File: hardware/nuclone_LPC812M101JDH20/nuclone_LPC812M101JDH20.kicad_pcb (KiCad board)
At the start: 2 copper layers, 48.3 x 48.3 mm, 102 parts, among them J1 JTAG_2X05, J2 Conn_01x02, J2 USB-ID, J3 nuclone_small_left, J4 nuclone_small_right, U1 MCP1702-MB, U1 USBLC6-2, U2 LPC812M101JDH20, U2 MCP1702-MB, U3 LPC812M101JDH20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

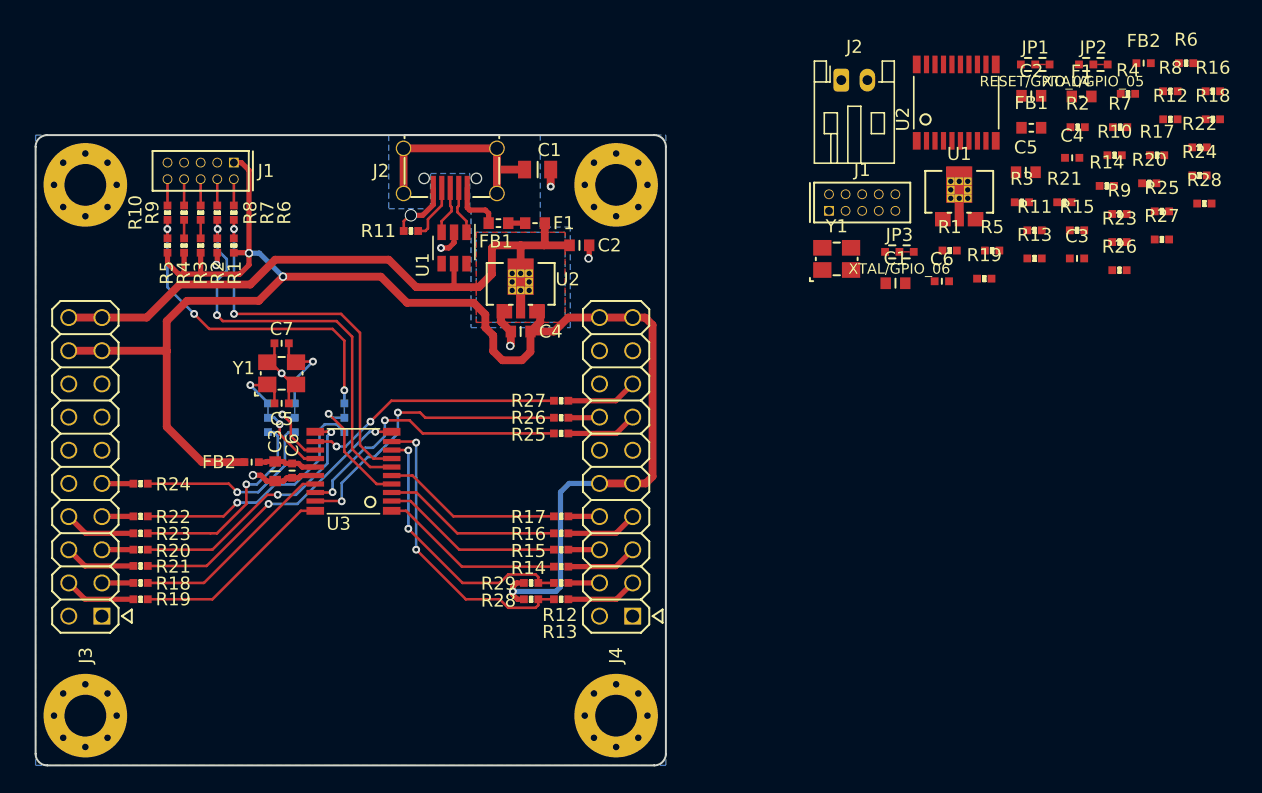
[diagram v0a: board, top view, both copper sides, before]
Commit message: newer footprints for nuclone generic, some updates to pcb
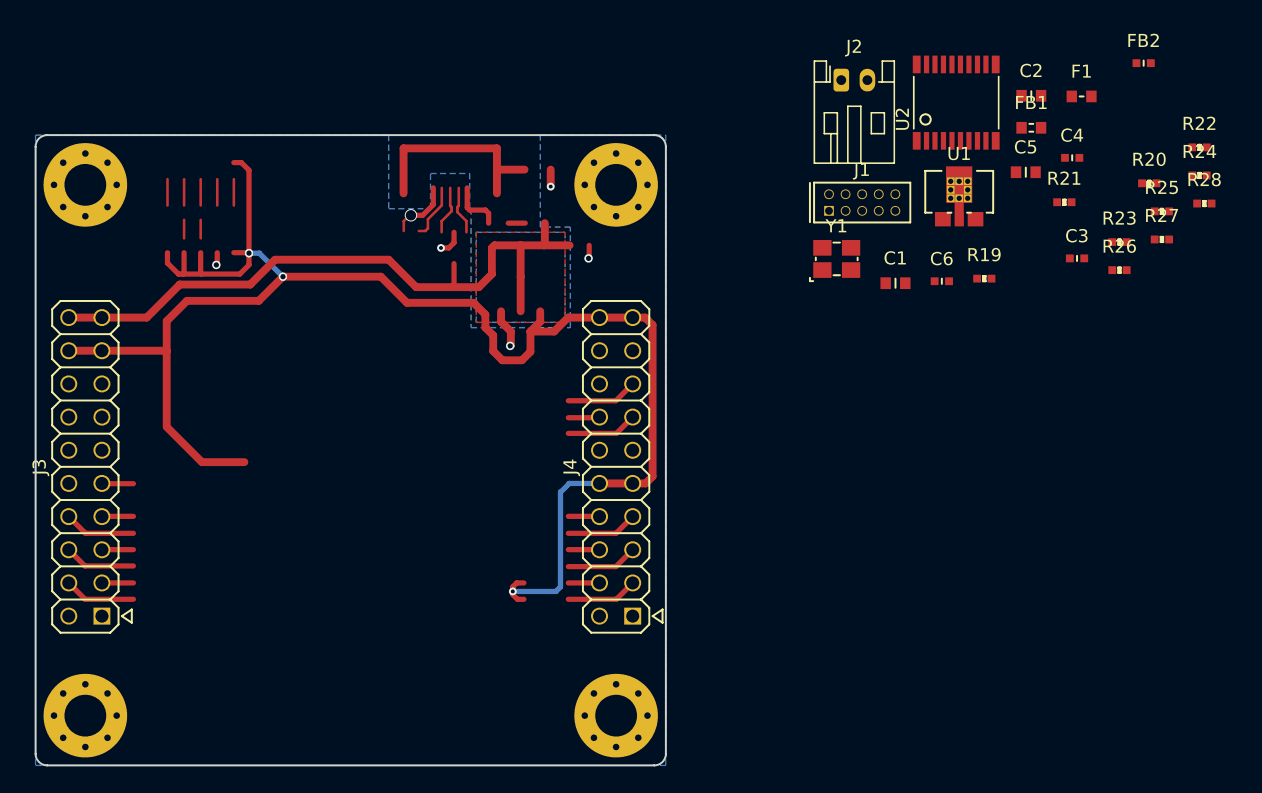
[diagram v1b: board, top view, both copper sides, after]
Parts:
- removed the C1 at (99.4, 63.6)
- removed the C2 at (102.6, 69.4)
- removed the C3 at (79.3, 86.7)
- removed the C4 at (98.1, 76.0)
- removed the C5 at (79.8, 81.5)
- removed the C6 at (80.6, 86.7)
- removed C7: 18p, SquantorRcl:C_0402
- removed the F1 at (99.2, 67.7)
- removed the FB1 at (96.4, 67.7)
- removed the FB2 at (77.5, 86.0)
- removed the J1 at (73.6, 63.7)
- removed the J2 at (92.7, 63.7)
- removed JP1 (x2): RESET/GPIO_04, SquantorSpecial:solder_jumper_3way_23conn
- removed JP2 (x2): XTAL/GPIO_05, SquantorSpecial:solder_jumper_3way_23conn
- removed JP3 (x2): XTAL/GPIO_06, SquantorSpecial:solder_jumper_3way_23conn
- removed R1, R10 (x2), R11, R12 (x2), R13 (x2), R14 (x2), R15 (x2), R16 (x2), R17, R18, R2, R3, R4, R5, R6 (x2), R7 (x2), R8 (x2), R9 (x2): 100, SquantorRcl:R_0402_hand
- removed R1, R4: 100K, SquantorRcl:R_0402_hand
- removed R11: 0, SquantorRcl:R_0402_hand
- removed R17, R18, R29: 2.2K, SquantorRcl:R_0402_hand
- removed the R19 at (69.0, 96.5)
- removed R2, R3, R5: 100k, SquantorRcl:R_0402_hand
- removed the R20 at (69.0, 92.7)
- removed the R21 at (69.0, 94.0)
- removed the R22 at (69.0, 90.2)
- removed the R23 at (69.0, 91.5)
- removed the R24 at (69.0, 87.7)
- removed the R25 at (101.2, 83.8)
- removed the R26 at (101.2, 82.6)
- removed the R27 at (101.2, 81.3)
- removed the R28 at (98.9, 96.5)
- removed the U1 at (93.0, 69.6)
- removed the U2 at (98.1, 72.7)
- removed U3: LPC812M101JDH20, SquantorIC:SOT360
- removed the Y1 at (79.8, 79.2)
- J3: footprint SquantorConnectorsNamed:Nuclone_20pin_gpio -> SquantorConnectorsNamed:nuclone_small_left
- J4: footprint SquantorConnectorsNamed:Nuclone_20pin_bus_analog -> SquantorConnectorsNamed:nuclone_small_right
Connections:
- net /MCU_RESET renamed /RESET
- C2 pad 1: /VBUS -> VSS
- C2 pad 2: VSS -> /VBUS
- J2 pad 1: (no net) -> VSS
- J2 pad 2: (no net) -> Net-(FB1-Pad2)
- J4 pad 19: (no net) -> /VDD
- J4 pad 20: (no net) -> /VDD
- U2 pad 1: /PIO0_17 -> (no net)
- U2 pad 10: /PIO0_16 -> (no net)
- U2 pad 11: /PIO0_15 -> (no net)
- U2 pad 12: /PIO0_1 -> (no net)
- U2 pad 13: /PIO0_9 -> (no net)
- U2 pad 14: /PIO0_8 -> (no net)
- U2 pad 17: /PIO0_7 -> (no net)
- U2 pad 18: /PIO0_6 -> (no net)
- U2 pad 19: /PIO0_0 -> (no net)
- U2 pad 2: /PIO0_13 -> (no net)
- U2 pad 20: /PIO0_14 -> (no net)
- U2 pad 3: /PIO0_12 -> (no net)
- U2 pad 4: /PIO0_5 -> (no net)
- U2 pad 5: /PIO0_4 -> (no net)
- U2 pad 8: /PIO0_11 -> (no net)
- U2 pad 9: /PIO0_10 -> (no net)
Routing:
- net (no net): track 5.46 -> 62.9 mm
- net /MCU_TCK: track 31.9 -> 0.00 mm, vias 2 -> 0
- net /MCU_TMS: track 29.6 -> 0.00 mm, vias 2 -> 0
- net /RESET: track 25.9 -> 0.00 mm, vias 3 -> 0
- net /LPC812M101JD20 base/PIO0_10: track 23.0 -> 0.00 mm, vias 2 -> 0
- net /LPC812M101JD20 base/PIO0_0: track 23.0 -> 0.00 mm, vias 2 -> 0
- net /LPC812M101JD20 base/PIO0_16: track 22.9 -> 0.00 mm, vias 2 -> 0
- net /LPC812M101JD20 base/PIO0_6: track 22.2 -> 0.00 mm, vias 2 -> 0
- net /LPC812M101JD20 base/PIO0_11: track 21.0 -> 0.00 mm, vias 2 -> 0
- net /LPC812M101JD20 base/PIO0_15: track 20.3 -> 0.00 mm, vias 2 -> 0
- net /LPC812M101JD20 base/PIO0_1: track 19.9 -> 0.00 mm, vias 2 -> 0
- net /LPC812M101JD20 base/GPIO_04_INT: track 19.6 -> 0.00 mm, vias 1 -> 0
- net /LPC812M101JD20 base/GPIO_05_INT: track 16.0 -> 0.00 mm, vias 1 -> 0
- net /LPC812M101JD20 base/PIO0_7: track 16.0 -> 0.00 mm
- net /LPC812M101JD20 base/PIO0_14: track 15.6 -> 0.00 mm
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
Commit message: updated footprints for the connectors (again)
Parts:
- removed R19, R22: 100K, SquantorRcl:R_0402_hand
- removed R20, R21, R23: 100k, SquantorRcl:R_0402_hand
- removed R24, R25, R26, R27, R28: 100, SquantorRcl:R_0402_hand
- J4: value nuclone_small_right -> Header-0254-2X10-H010
- moved F1 50.4 mm to (91.0, 64.0), turned to 270 degrees
- moved FB1 46.7 mm to (91.0, 67.0), turned to 270 degrees
- moved J2 28.0 mm to (96.9, 67.7), turned to 180 degrees
- turned J3 to 270 degrees
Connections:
- J1 pad 10: Net-(J1-Pad10) -> (no net)
- J1 pad 2: Net-(J1-Pad2) -> (no net)
- J1 pad 4: Net-(J1-Pad4) -> (no net)
- J1 pad 6: Net-(J1-Pad6) -> (no net)
- J1 pad 8: Net-(J1-Pad8) -> (no net)
- J3 pad 1: VSS -> /VDD
- J3 pad 17: /VDD -> (no net)
- J3 pad 18: /VDD -> (no net)
- J3 pad 19: /VBUS -> (no net)
- J3 pad 2: VSS -> /VDD
- J3 pad 20: /VBUS -> (no net)
- J3 pad 3: (no net) -> /VBUS
- J3 pad 4: (no net) -> /VBUS
- J3 pad 5: (no net) -> VSS
- J3 pad 6: (no net) -> VSS
- J4 pad 1: VSS -> (no net)
- J4 pad 17: (no net) -> VSS
- J4 pad 18: (no net) -> VSS
- J4 pad 2: VSS -> (no net)
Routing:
- net /VDD: track 126.5 -> 0.00 mm, vias 3 -> 0
- net (no net): track 62.9 -> 0.17 mm
- net /VBUS: track 52.2 -> 0.00 mm
- net Net-(C1-Pad1): track 16.2 -> 0.00 mm
- net VSS: track 13.1 -> 0.00 mm, vias 6 -> 0
- net Net-(J2-Pad4): track 4.32 -> 0.00 mm
- net Net-(FB1-Pad2): track 4.08 -> 0.00 mm
- net /USB input/USB_IN_D+: track 3.76 -> 0.00 mm
- net /USB input/USB_IN_D-: track 3.73 -> 0.00 mm
- net Net-(J1-Pad8): track 2.02 -> 0.00 mm
- net Net-(J1-Pad6): track 2.02 -> 0.00 mm
- net Net-(J1-Pad4): track 2.02 -> 0.00 mm
- net Net-(J1-Pad2): track 2.02 -> 0.00 mm
- net Net-(J1-Pad10): track 2.02 -> 0.00 mm
- net /MCU_TDO: track 1.41 -> 0.00 mm
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- removed copper zone on B.Cu, net /VBUS
- removed copper zone on F.Cu, net /VBUS

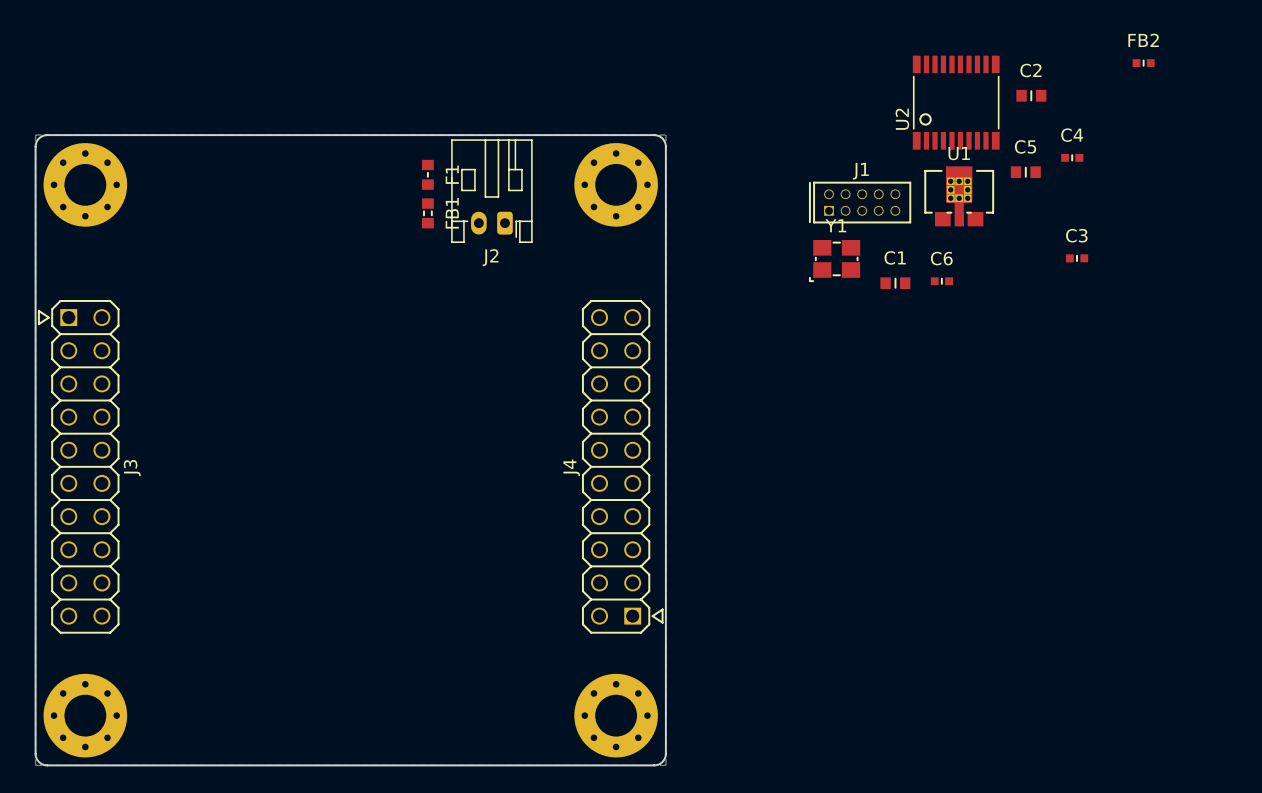
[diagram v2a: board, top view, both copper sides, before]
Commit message: additional gpios schematic drawn
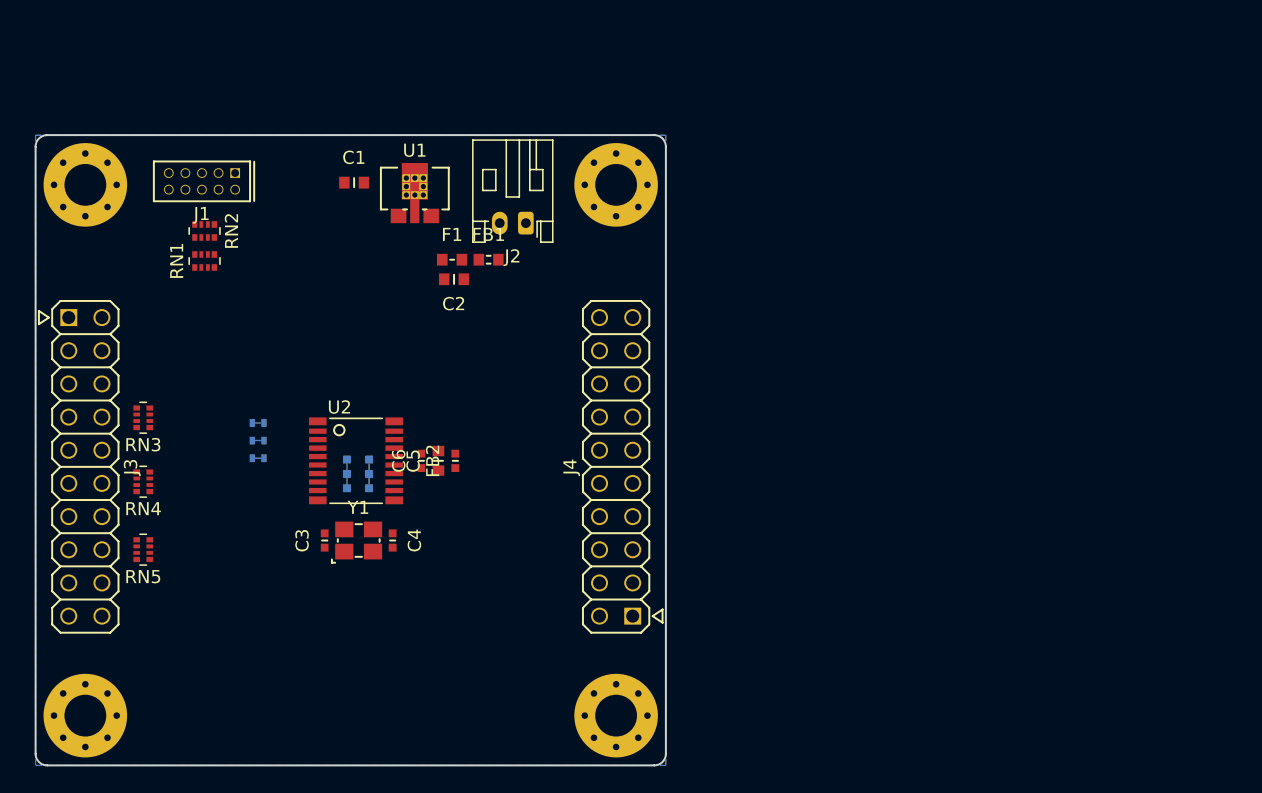
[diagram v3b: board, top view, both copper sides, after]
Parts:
- added JP1: TCK/PIO, SquantorSpecial:solder_jumper_2way_conn, B.Cu at (78.0, 85.7)
- added JP2: TMS/PIO, SquantorSpecial:solder_jumper_2way_conn, B.Cu at (78.0, 83.0)
- added JP3: RESET/PIO, SquantorSpecial:solder_jumper_2way_conn, B.Cu at (78.0, 84.3)
- added JP4: XTAL/PIO, SquantorSpecial:solder_jumper_3way_123conn, B.Cu at (86.5, 86.9)
- added JP5: XTAL/PIO, SquantorSpecial:solder_jumper_3way_123conn, B.Cu at (84.8, 86.9)
- added RN1: 47K, Resistor_SMD:R_Array_Convex_4x0402, F.Cu at (73.9, 70.6)
- added RN2: 100, Resistor_SMD:R_Array_Convex_4x0402, F.Cu at (73.9, 68.3)
- added RN3: 100, Resistor_SMD:R_Array_Convex_4x0402, F.Cu at (69.2, 82.6)
- added RN4: 100, Resistor_SMD:R_Array_Convex_4x0402, F.Cu at (69.2, 87.5)
- added RN5: 100, Resistor_SMD:R_Array_Convex_4x0402, F.Cu at (69.2, 92.7)
- J4: value Header-0254-2X10-H010 -> nuclone_small_right
- moved C3 61.5 mm to (83.1, 92.0), turned to 90 degrees
- moved FB2 60.9 mm to (93.1, 85.9), turned to 90 degrees
- moved C4 59.7 mm to (88.3, 92.0), turned to 270 degrees
- moved U2 53.5 mm to (85.5, 85.9), turned to 270 degrees
- moved J1 50.6 mm to (73.7, 64.5), turned to 180 degrees
- moved C5 50.1 mm to (91.8, 85.9), turned to 90 degrees
- moved C2 46.4 mm to (93.0, 72.0), turned to 180 degrees
- moved Y1 42.5 mm to (85.7, 92.0)
- moved C1 42.2 mm to (85.3, 64.6)
- moved C6 42.2 mm to (90.5, 85.9), turned to 90 degrees
- moved U1 41.7 mm to (90.0, 65.4)
- moved F1 6.76 mm to (92.8, 70.5), turned to 0 degrees
- moved FB1 5.85 mm to (95.7, 70.5), turned to 0 degrees
- moved J2 1.60 mm to (98.5, 67.7)
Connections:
- J1 pad 10: (no net) -> Net-(J1-Pad10)
- J1 pad 2: (no net) -> Net-(J1-Pad2)
- J1 pad 4: (no net) -> Net-(J1-Pad4)
- J1 pad 6: (no net) -> Net-(J1-Pad6)
- J3 pad 10: (no net) -> /PIO0_5_OUT
- J3 pad 11: (no net) -> /PIO0_4_OUT
- J3 pad 12: (no net) -> /PIO0_3_OUT
- J3 pad 13: (no net) -> /PIO0_2_OUT
- J3 pad 14: (no net) -> /PIO0_11_OUT
- J3 pad 15: (no net) -> /PIO0_10_OUT
- J3 pad 16: (no net) -> /PIO0_16_OUT
- J3 pad 17: (no net) -> /GPIO_10
- J3 pad 18: (no net) -> /GPIO_11
- J3 pad 7: (no net) -> /PIO0_17_OUT
- J3 pad 8: (no net) -> /PIO0_13_OUT
- J3 pad 9: (no net) -> /PIO0_12_OUT
- U2 pad 1: (no net) -> /PIO0_17_MCU
- U2 pad 10: (no net) -> /PIO0_16_MCU
- U2 pad 13: (no net) -> /PIO0_9_MCU
- U2 pad 14: (no net) -> /PIO0_8_MCU
- U2 pad 2: (no net) -> /PIO0_13_MCU
- U2 pad 3: (no net) -> /PIO0_12_MCU
- U2 pad 4: (no net) -> /PIO0_5_MCU
- U2 pad 5: (no net) -> /PIO0_4_MCU
- U2 pad 6: (no net) -> /PIO0_3_MCU
- U2 pad 7: (no net) -> /PIO0_2_MCU
- U2 pad 8: (no net) -> /PIO0_11_MCU
- U2 pad 9: (no net) -> /PIO0_10_MCU

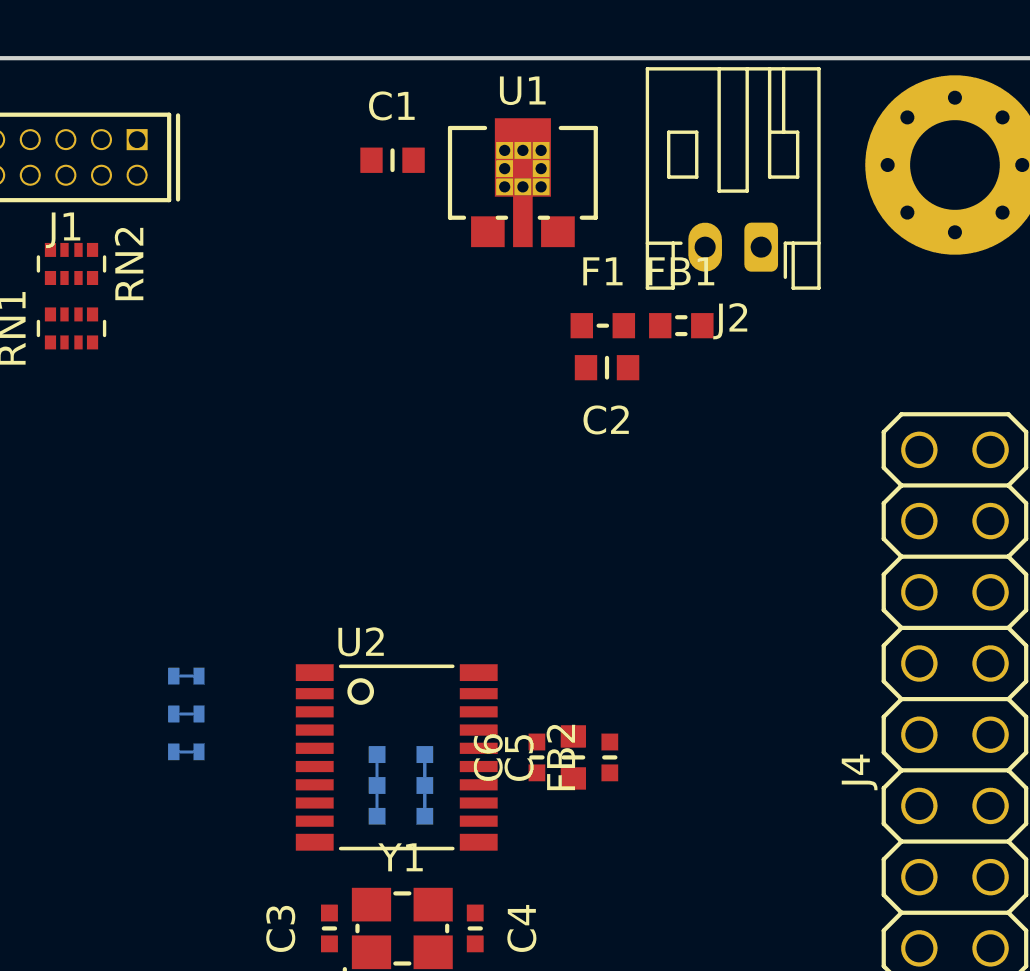
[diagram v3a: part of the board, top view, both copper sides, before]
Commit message: added all gpio's
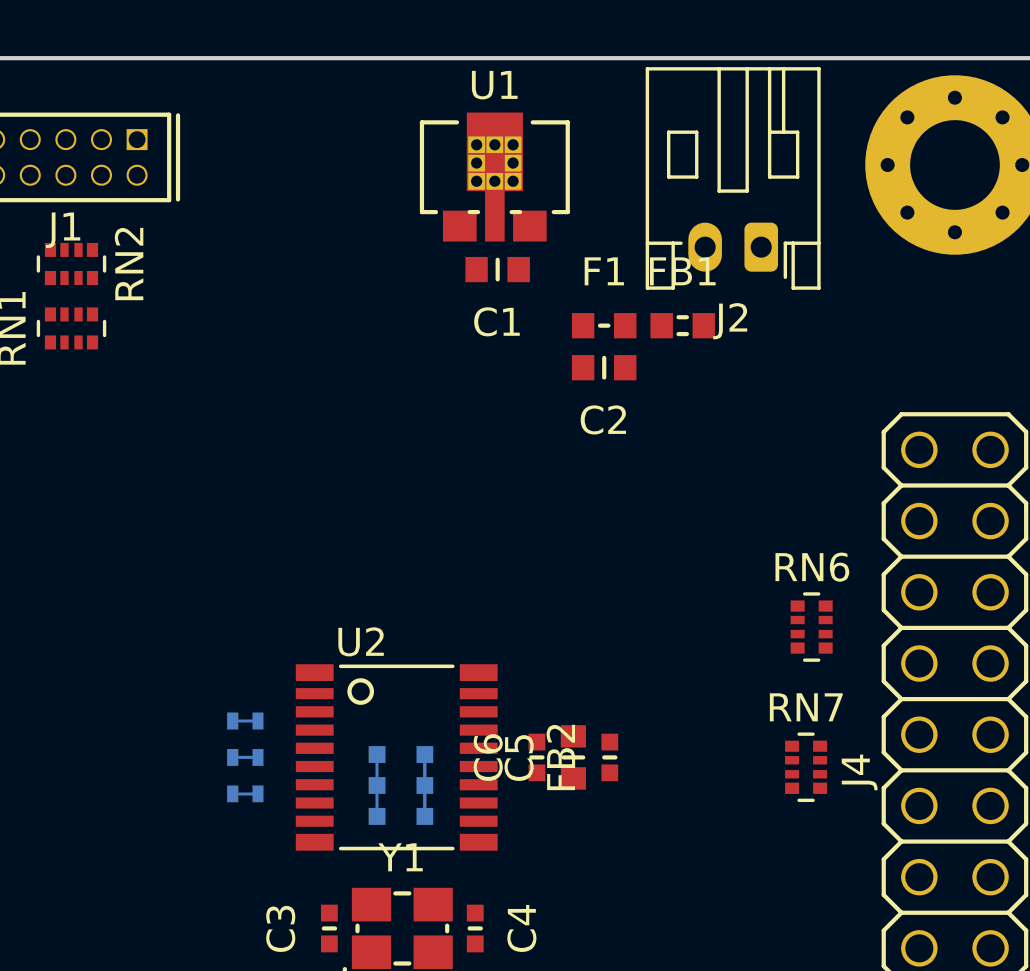
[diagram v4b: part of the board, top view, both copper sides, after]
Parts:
- added RN6: 100, Resistor_SMD:R_Array_Convex_4x0402, F.Cu at (100.3, 81.2)
- added RN7: 100, Resistor_SMD:R_Array_Convex_4x0402, F.Cu at (100.1, 86.2)
- moved C1 5.41 mm to (89.1, 68.5), turned to 180 degrees
- moved JP2 4.70 mm to (80.1, 87.2)
- moved JP3 2.11 mm to (80.1, 84.6)
- moved JP1 2.11 mm to (80.1, 85.9)
- moved U1 1.02 mm to (89.0, 65.2)
- moved C2 0.10 mm to (92.9, 72.0)
- moved F1 0.05 mm to (92.9, 70.5)
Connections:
- J4 pad 10: (no net) -> /PIO0_1_OUT
- J4 pad 11: (no net) -> /PIO0_9_OUT
- J4 pad 12: (no net) -> /PIO0_8_OUT
- J4 pad 13: (no net) -> /PIO0_7_OUT
- J4 pad 14: (no net) -> /PIO0_6_OUT
- J4 pad 15: (no net) -> /PIO0_0_OUT
- J4 pad 16: (no net) -> /PIO0_14_OUT
- J4 pad 9: (no net) -> /PIO0_15_OUT
- JP4 pad 1: (no net) -> /PIO0_8
- JP5 pad 1: (no net) -> /PIO0_9
- U2 pad 11: (no net) -> /PIO0_15_MCU
- U2 pad 12: (no net) -> /PIO0_1_MCU
- U2 pad 17: (no net) -> /PIO0_7_MCU
- U2 pad 18: (no net) -> /PIO0_6_MCU
- U2 pad 19: (no net) -> /PIO0_0_MCU
- U2 pad 20: (no net) -> /PIO0_14_MCU
